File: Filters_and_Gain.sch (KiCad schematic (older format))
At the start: 25 parts, among them U4 OPA388, U5 OPA388, U6 OPA388

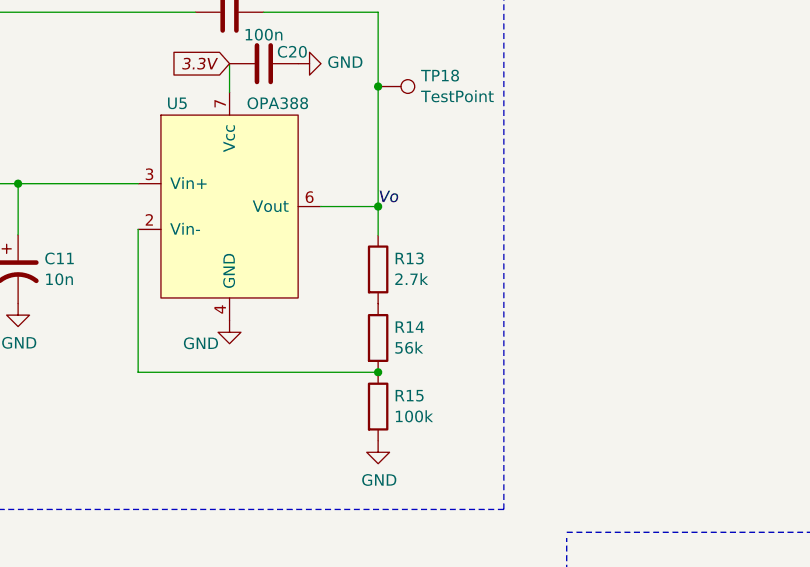
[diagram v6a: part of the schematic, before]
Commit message: #13 and #5 - Updated circuits for 3.3V power rail
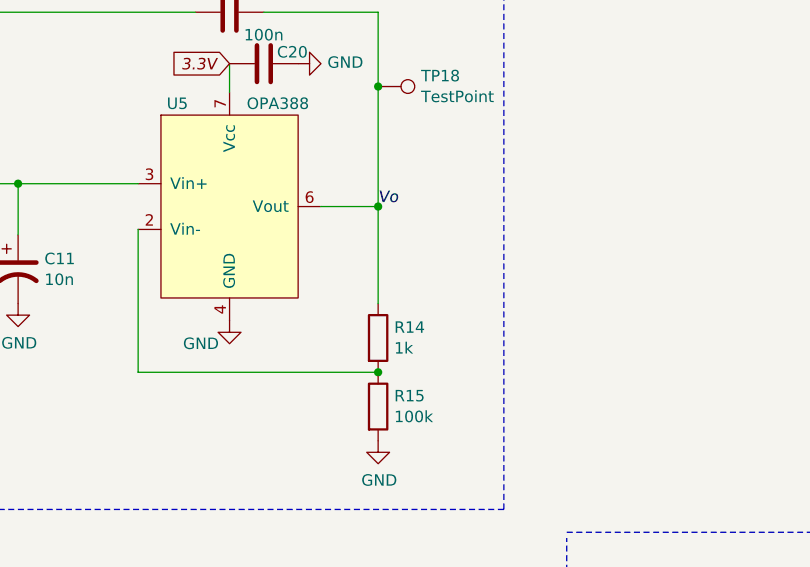
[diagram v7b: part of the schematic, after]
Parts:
- removed R13: 2.7k, Resistor_SMD:R_0805_2012Metric_Pad1.20x1.40mm_HandSolder, symbol Device:R
- R14: value 56k -> 1k
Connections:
- net Vo: now also R14.1
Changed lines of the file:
@@
 P 5625 2875
 F 0 "R14" H 5695 2921 50  0000 L CNN
-F 1 "56k" H 5695 2830 50  0000 L CNN
+F 1 "1k" H 5695 2830 50  0000 L CNN
 F 2 "Resistor_SMD:R_0805_2012Metric_Pad1.20x1.40mm_HandSolder" V 5555 2875 50  0001 C CNN
 F 3 "~" H 5625 2875 50  0001 C CNN
@@
 	1    0    0    -1
 $EndComp
-$Comp
-L Device:R R13
-U 1 1 5FA2106F
-P 5625 2575
-F 0 "R13" H 5695 2621 50  0000 L CNN
-F 1 "2.7k" H 5695 2530 50  0000 L CNN
-F 2 "Resistor_SMD:R_0805_2012Metric_Pad1.20x1.40mm_HandSolder" V 5555 2575 50  0001 C CNN
-F 3 "~" H 5625 2575 50  0001 C CNN
-	1    5625 2575
-	1    0    0    -1
-$EndComp
 Connection ~ 5625 3025
 Wire Wire Line
 	5625 1450 5625 1775
-Wire Wire Line
-	5625 2300 5625 2425
 Connection ~ 5625 2300
 Wire Wire Line
@@
 	0    1    1    0
 $EndComp
+Wire Wire Line
+	5625 2300 5625 2725
 $EndSCHEMATC
